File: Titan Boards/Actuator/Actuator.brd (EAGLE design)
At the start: 101.6 x 101.6 mm, 74 parts, among them Y1 12MHz, Y3 32.768kHz

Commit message: actuator board work TL
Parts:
- moved D8 19.8 mm to (45.4, 37.4)
- moved D9 18.8 mm to (45.4, 41.6)
- moved ARMED 12.3 mm to (36.0, 28.8), turned to 270 degrees
- moved Q17 11.3 mm to (51.5, 37.7), turned to 180 degrees
- moved D10 11.2 mm to (32.5, 32.9)
- moved C5 9.98 mm to (40.9, 25.7), turned to 90 degrees
- moved R20 7.11 mm to (32.2, 29.7)
- moved R21 5.12 mm to (34.2, 25.8)
- moved Q12 3.30 mm to (51.5, 41.7), turned to 180 degrees
- moved U$6 0.22 mm to (32.9, 19.2)
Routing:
- net +12V: track 19.1 -> 58.3 mm, vias 0 -> 2
- net +24V: track 109.0 -> 146.8 mm
- net ARM_TORPEDO: track 13.6 -> 50.3 mm, vias 0 -> 4
- net DROPPER1_GATE: track 14.0 -> 41.7 mm, vias 0 -> 4
- net DROPPER2_GATE: track 12.5 -> 34.8 mm, vias 0 -> 2
- net AGND: track 86.1 -> 104.0 mm, vias 21 -> 23
- net N$26: track 0.00 -> 12.8 mm
- net DROPPER1: track 0.00 -> 4.36 mm
- net DROPPER2: track 0.00 -> 4.36 mm
- net N$35: track 12.3 -> 14.8 mm, vias 0 -> 2
- net N$10: track 0.00 -> 2.46 mm

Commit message: actuator board TL
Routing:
- net +12V: track 58.3 -> 80.3 mm, vias 2 -> 0
- net ARM_TORPEDO: vias 4 -> 2
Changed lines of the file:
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@@
 <contactref element="U$6" pad="P$2"/>
 <contactref element="POWER_INPUT" pad="4"/>
-<wire x1="33.8912" y1="17.6512" x2="23.4341" y2="17.6512" width="1.5" layer="1"/>
-<wire x1="21.5758" y1="19.5095" x2="23.4341" y2="17.6512" width="1.5" layer="1"/>
-<wire x1="33.8912" y1="17.6512" x2="35.396" y2="19.156" width="1.5" layer="1"/>
+<wire x1="35.396" y1="19.156" x2="33.2008" y2="21.3512" width="1.5" layer="1"/>
+<wire x1="33.2008" y1="21.3512" x2="23.4175" y2="21.3512" width="1.5" layer="1"/>
+<wire x1="21.5758" y1="19.5095" x2="23.4175" y2="21.3512" width="1.5" layer="1"/>
 </signal>
 <signal name="N$26">
@@
 <wire x1="43.05" y1="46.85" x2="43" y2="46.8" width="0.1524" layer="1"/>
 <wire x1="43.05" y1="46.85" x2="43.05" y2="44.45" width="0.1524" layer="1"/>
-<wire x1="39.6" y1="41" x2="39.6" y2="38.4" width="0.1524" layer="1"/>
-<via x="39.6" y="38.4" extent="1-16" drill="0.35"/>
-<wire x1="39.6" y1="38.4" x2="39.6" y2="36.3" width="0.1524" layer="16"/>
-<via x="39.6" y="36.3" extent="1-16" drill="0.35"/>
-<wire x1="39.6" y1="36.3" x2="39.6" y2="29.7" width="0.1524" layer="1"/>
 <wire x1="39.6" y1="29.7" x2="39.4" y2="29.5" width="0.1524" layer="1"/>
 <via x="39.4" y="29.5" extent="1-16" drill="0.35"/>
@@
 <wire x1="38" y1="19.22" x2="37.936" y2="19.156" width="0.1524" layer="1"/>
 <wire x1="38" y1="22.4" x2="38" y2="19.22" width="0.1524" layer="1"/>
+<wire x1="39.6" y1="41" x2="39.6" y2="29.7" width="0.1524" layer="1"/>
 </signal>
 <signal name="N$10">
@@
 <contactref element="CLAW_CONNECTOR" pad="2"/>
 <contactref element="POWER_INPUT" pad="2"/>
-<wire x1="16.064" y1="19.5095" x2="17.564" y2="19.5095" width="0.8" layer="1"/>
 <wire x1="16.028" y1="31.1095" x2="13.9" y2="28.9815" width="0.8" layer="1"/>
 <wire x1="16.064" y1="19.5095" x2="16.064" y2="19.6095" width="0.8" layer="1"/>
 <wire x1="16.064" y1="19.6095" x2="13.9" y2="21.7735" width="0.8" layer="1"/>
 <wire x1="13.9" y1="28.9815" x2="13.9" y2="21.7735" width="0.8" layer="1"/>
-<wire x1="26.3" y1="28.2455" x2="26.3" y2="36.1" width="0.8" layer="1"/>
-<wire x1="17.564" y1="19.5095" x2="26.3" y2="28.2455" width="0.8" layer="1"/>
 <wire x1="43.196" y1="41.568" x2="41.3" y2="39.672" width="0.8" layer="1"/>
 <wire x1="41.3" y1="39.26" x2="43.196" y2="37.364" width="0.8" layer="1"/>
 <wire x1="41.3" y1="39.672" x2="41.3" y2="39.26" width="0.8" layer="1"/>
-<wire x1="27.6" y1="37.4" x2="30.5" y2="37.4" width="0.8" layer="1"/>
-<via x="30.5" y="37.4" extent="1-16" drill="0.35"/>
-<wire x1="30.5" y1="37.4" x2="34.4" y2="37.4" width="0.8" layer="16"/>
-<via x="34.4" y="37.4" extent="1-16" drill="0.35"/>
-<wire x1="34.4" y1="37.4" x2="43.16" y2="37.4" width="0.8" layer="1"/>
 <wire x1="43.16" y1="37.4" x2="43.196" y2="37.364" width="0.8" layer="1"/>
-<wire x1="26.3" y1="36.1" x2="27.6" y2="37.4" width="0.8" layer="1"/>
+<wire x1="53.3" y1="23" x2="43.196" y2="33.104" width="0.8" layer="1"/>
+<wire x1="43.196" y1="33.104" x2="43.196" y2="37.364" width="0.8" layer="1"/>
+<wire x1="16.064" y1="19.5095" x2="17.5905" y2="19.5095" width="0.8" layer="1"/>
+<wire x1="17.5905" y1="19.5095" x2="19.8" y2="17.3" width="0.8" layer="1"/>
+<wire x1="19.8" y1="17.3" x2="51.1" y2="17.3" width="0.8" layer="1"/>
+<wire x1="51.1" y1="17.3" x2="53.3" y2="19.5" width="0.8" layer="1"/>
+<wire x1="53.3" y1="19.5" x2="53.3" y2="23" width="0.8" layer="1"/>
 </signal>
 <signal name="DROPPER1">

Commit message: Titan Actuator Review Copy
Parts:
- moved C4 6.94 mm to (84.8, 67.0)
- moved R2 4.31 mm to (14.0, 58.9), turned to 180 degrees
- moved R30 0.15 mm to (63.2, 42.9), turned to 180 degrees
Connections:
- net +3V3: now also U$1.43
- net EXTRA4: no longer U$1.43
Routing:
- net EXTRA4: track 62.6 -> 0.00 mm
- net +3V3: track 205.5 -> 237.0 mm, vias 3 -> 4
- net RESET: track 66.8 -> 80.9 mm, vias 1 -> 2
- net AGND: track 104.0 -> 94.1 mm, vias 23 -> 27
- net DROPPER1_GATE: track 41.7 -> 38.0 mm, vias 4 -> 2
- net +24V: track 146.8 -> 149.4 mm
- net ARM_TORPEDO: track 50.3 -> 52.3 mm, vias 2 -> 0
- net N$26: track 12.8 -> 11.1 mm
- net +12V: track 80.3 -> 78.7 mm
- net DROPPER2_GATE: track 34.8 -> 33.4 mm
- net N$30: track 20.6 -> 21.8 mm
- net USB_ID: track 1.84 -> 2.45 mm

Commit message: Start of board review change, Actuator
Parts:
- added C1, C12: 0.1uF, rcl:C0603
- added C10: 1uF, rcl:C0603
- added C11, C6: 0.5uF, rcl:C0603
- moved C3 32.3 mm to (59.5, 64.5), turned to 90 degrees
- moved C2 25.9 mm to (59.5, 60.1)
- moved Y1 23.3 mm to (63.0, 62.1), turned to 90 degrees
- moved RESET_SWITCH 19.9 mm to (72.2, 49.4), turned to 0 degrees
- moved R27 6.57 mm to (65.8, 49.4)
- moved R30 6.57 mm to (61.7, 49.3)
- moved C13 5.40 mm to (59.4, 64.5), flipped to the bottom
- moved C9 5.30 mm to (59.5, 60.1), flipped to the bottom
- moved U$6 5.00 mm to (27.9, 19.2)
- moved Y3 0.22 mm to (61.7, 62.1), flipped to the bottom
- moved LIGHT1 0.05 mm to (61.7, 87.4)
- moved LIGHT8 0.05 mm to (41.4, 87.4)
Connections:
- net +12V: no longer D8.C, D9.C
- net +3V3: now also C1.1, C10.1, C11.1, C12.1, C6.1
- net +5V: now also D8.C, D9.C
- net AGND: now also C1.2, C10.2, C11.2, C12.2, C6.2, USB_ID/USB_DP/USB_DN.S1, USB_ID/USB_DP/USB_DN.S2, USB_ID/USB_DP/USB_DN.S3, USB_ID/USB_DP/USB_DN.S4; no longer MARKER_DROPPER.1, MARKER_DROPPER.3
- net DROPPER1: now also MARKER_DROPPER.1
- net DROPPER2: now also MARKER_DROPPER.3
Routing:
- net +12V: track 78.7 -> 13.5 mm
- net DROPPER1: track 4.36 -> 37.3 mm, vias 0 -> 1
- net N$3: track 36.5 -> 6.59 mm
- net DROPPER2: track 4.36 -> 32.2 mm, vias 0 -> 1
- net +3V3: track 237.0 -> 211.9 mm, vias 4 -> 10
- net N$2: track 32.6 -> 11.4 mm
- net RESET: track 80.9 -> 64.6 mm
- net AGND: track 94.1 -> 84.1 mm, vias 27 -> 25
- net N$30: track 21.8 -> 15.1 mm
- net +5V: track 73.1 -> 66.8 mm, vias 1 -> 3
- net V+: track 15.5 -> 10.5 mm
- net N$12: track 8.07 -> 5.91 mm, vias 0 -> 1
- net PWM_CLAW: track 64.3 -> 62.5 mm
- net ARM_TORPEDO: track 52.3 -> 53.9 mm
- net N$26: track 11.1 -> 9.72 mm
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
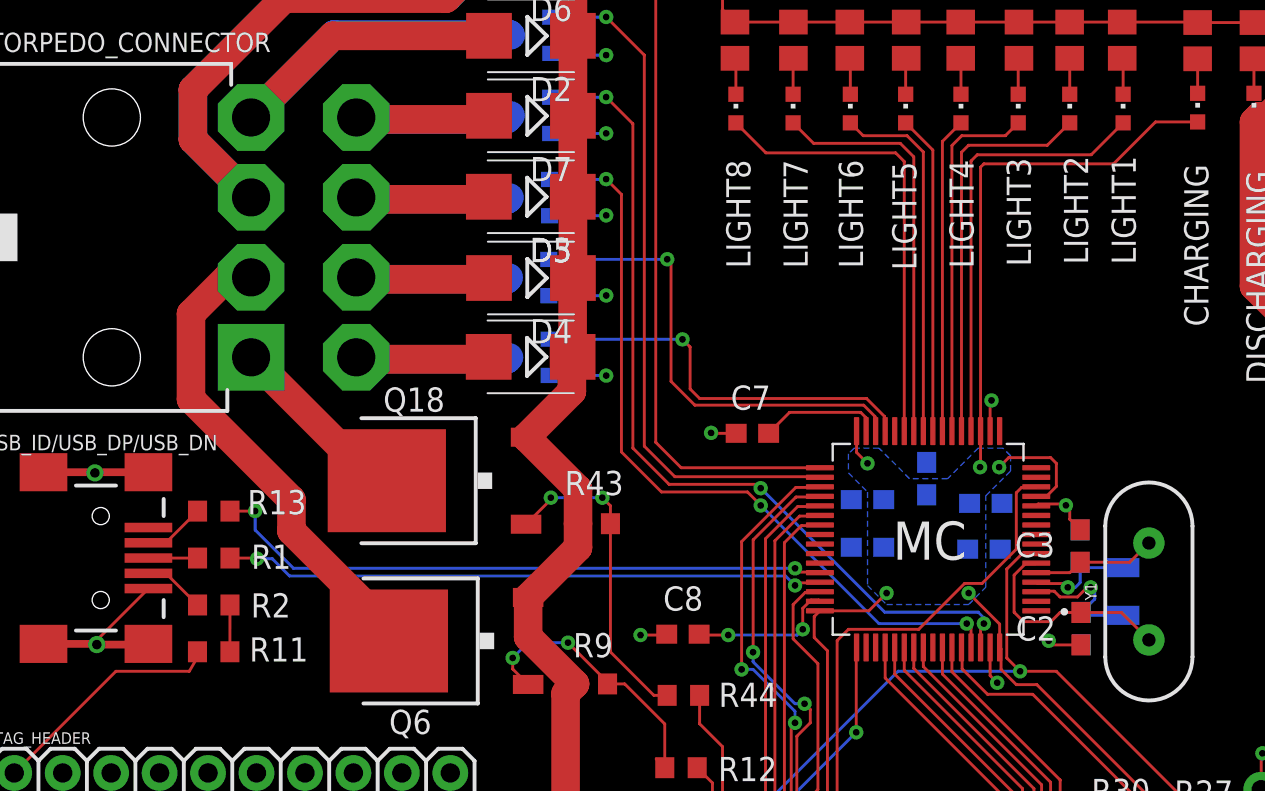
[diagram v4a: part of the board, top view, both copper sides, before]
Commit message: Actuator VBUS converter, crystal changes
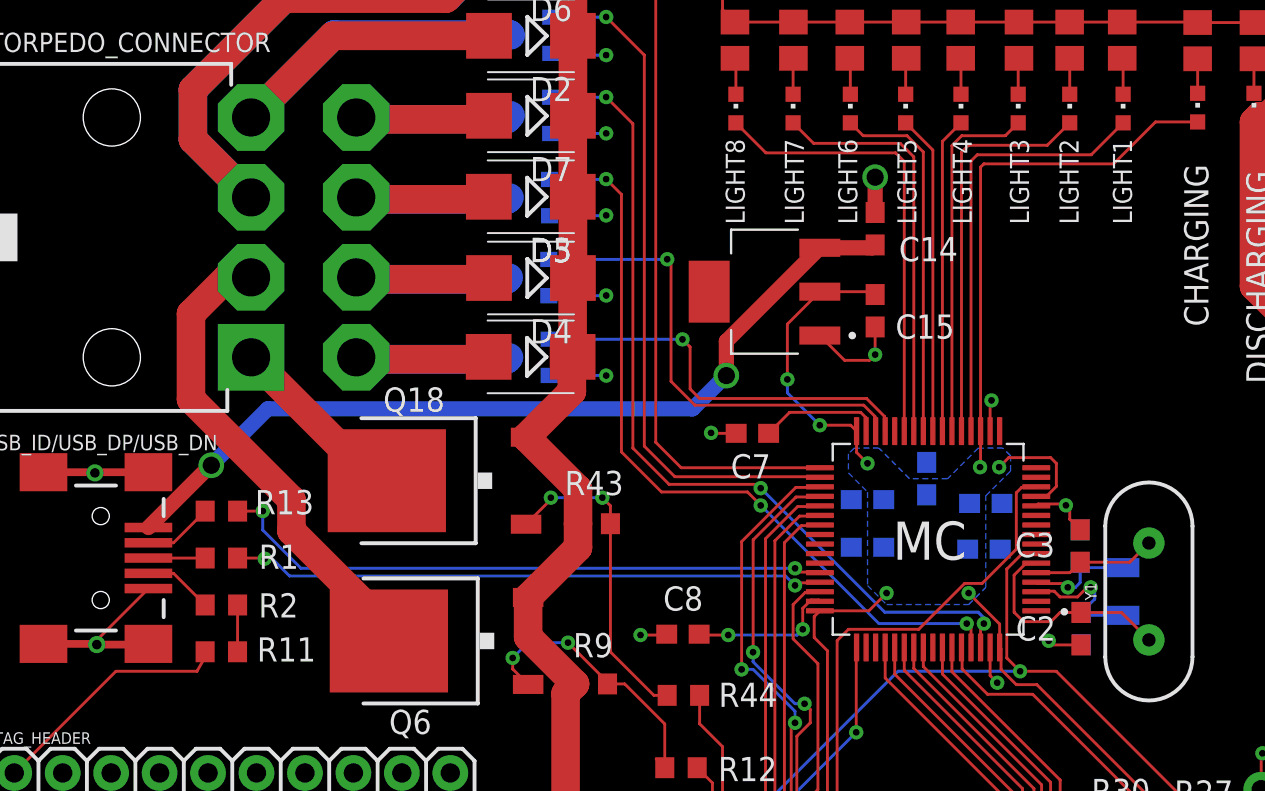
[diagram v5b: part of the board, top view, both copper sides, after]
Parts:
- added C14, C15: 10uF, rcl:C0603
- added VR1: LM1117IMPX-3.3/NOPB, LM1117IMPX-3.3_NOPB:VREG_LM1117IMPX-3.3/NOPB
- Y1: value 12MHz -> 16MHz
- moved R1 0.40 mm to (14.4, 63.8)
- moved R11 0.40 mm to (14.4, 61.4)
- moved R13 0.40 mm to (14.4, 66.3)
- moved R2 0.40 mm to (14.4, 58.9)
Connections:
- net +3V3: now also C15.1, VR1.2
- net AGND: now also C14.2, C15.2, VR1.1
- net VBUS: now also C14.1, VR1.3
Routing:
- net VBUS: track 0.00 -> 45.3 mm, vias 0 -> 2
- net +3V3: track 211.9 -> 225.7 mm, vias 10 -> 12
- net AGND: track 84.1 -> 91.0 mm, vias 25 -> 27

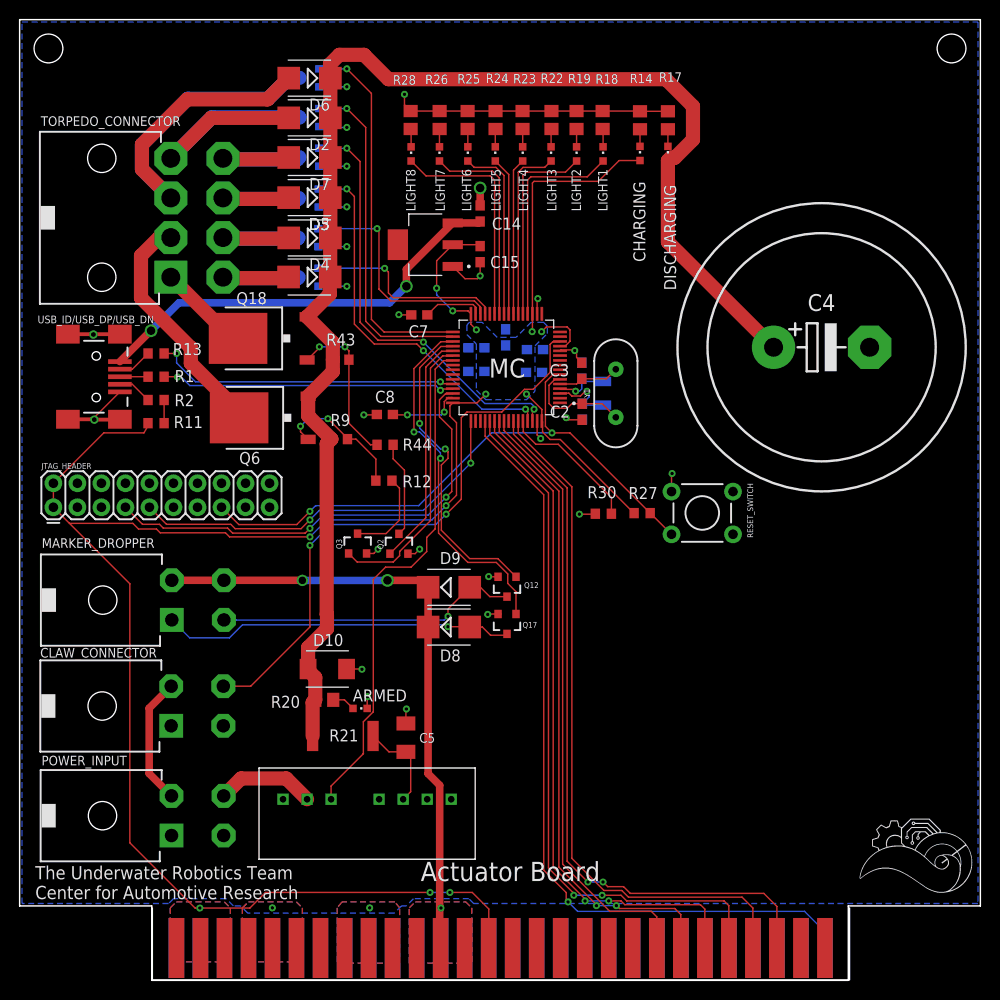
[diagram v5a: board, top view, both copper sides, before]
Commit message: Actuator trace width, start of changing FETs
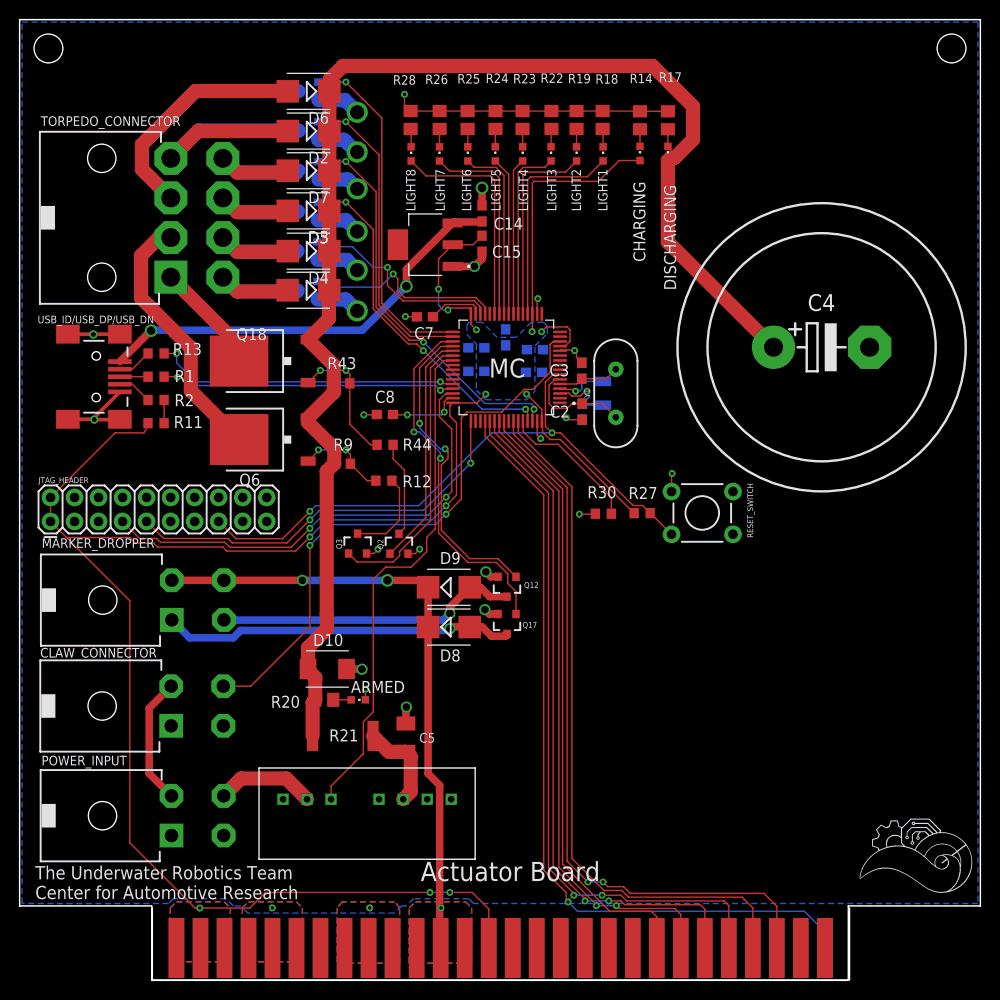
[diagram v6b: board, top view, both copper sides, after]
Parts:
- moved R9 2.62 mm to (34.1, 54.6)
- moved R43 2.50 mm to (34.1, 63.1)
- moved Q18 2.40 mm to (25.7, 65.5)
- moved Q6 2.30 mm to (25.7, 57.2)
- moved JTAG_HEADER 1.53 mm to (3.27, 48.5)
- moved D2 1.40 mm to (30.6, 89.8)
- moved D4 1.40 mm to (30.6, 77.1)
- moved D6 1.40 mm to (30.6, 94.0)
- moved Q1 1.40 mm to (30.6, 89.8)
- moved Q13 1.40 mm to (30.5, 77.1)
- moved Q14 1.40 mm to (30.6, 85.6)
- moved Q5 1.40 mm to (30.5, 73.0)
- moved D3 1.40 mm to (30.5, 73.0)
- moved D5 1.40 mm to (30.6, 81.4)
- moved D7 1.40 mm to (30.6, 85.6)
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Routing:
- net AGND: track 91.0 -> 99.5 mm
- net N$35: track 14.8 -> 10.3 mm
- net COIL_1_GATE: track 40.8 -> 37.3 mm
- net COIL_2_GATE: track 45.6 -> 42.3 mm
- net COIL_S_GATE: track 36.1 -> 32.9 mm
- net COIL_4_GATE: track 24.9 -> 21.9 mm
- net COIL_5_GATE: track 39.6 -> 36.6 mm
- net N$33: track 16.8 -> 14.2 mm
- net TORPEDO2: track 25.4 -> 27.7 mm
- net TORPEDO1: track 9.80 -> 11.9 mm
- net +3V3: track 225.7 -> 227.5 mm
- net AGND1: track 2.91 -> 4.64 mm
- net +24V: track 149.4 -> 147.7 mm
- net COIL_S: track 29.7 -> 28.3 mm
- net COIL_5: track 51.9 -> 50.5 mm
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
